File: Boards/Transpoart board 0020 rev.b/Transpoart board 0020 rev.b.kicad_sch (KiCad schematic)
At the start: 81 parts, among them J1 CEC card edge connector large, U1 6821, U1 TR1602, U10 LM311, U11 LM741, U12 LM311, U3 DM8602N, U4 7410, U4 ULN2003A, U5 74LS74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

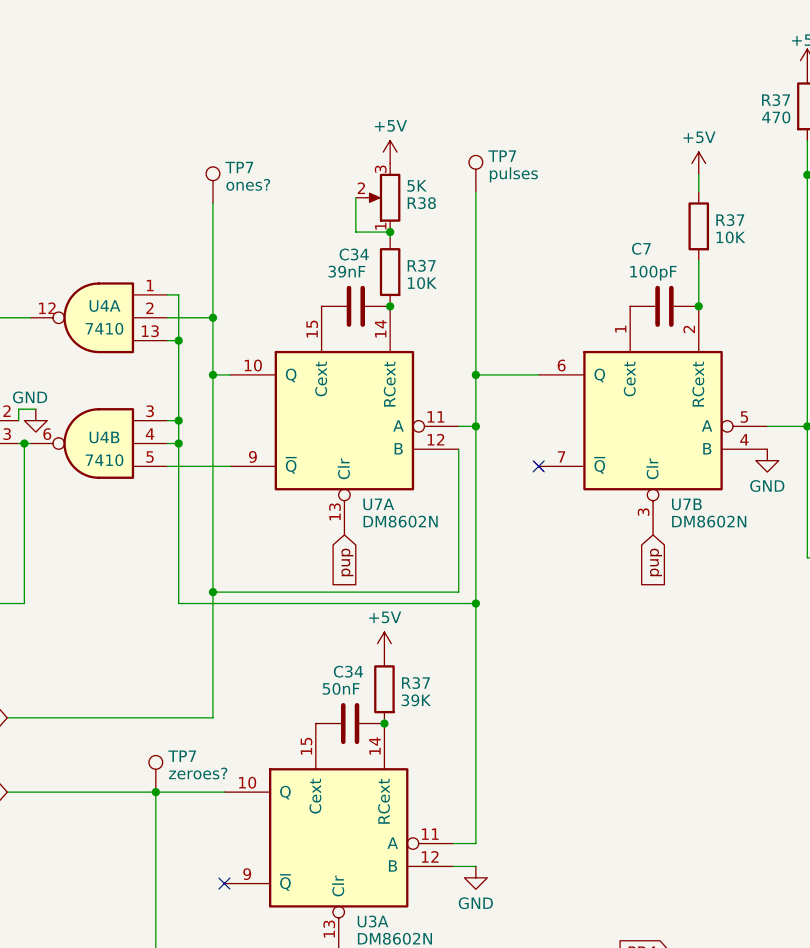
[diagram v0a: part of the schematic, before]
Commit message: revised test point names
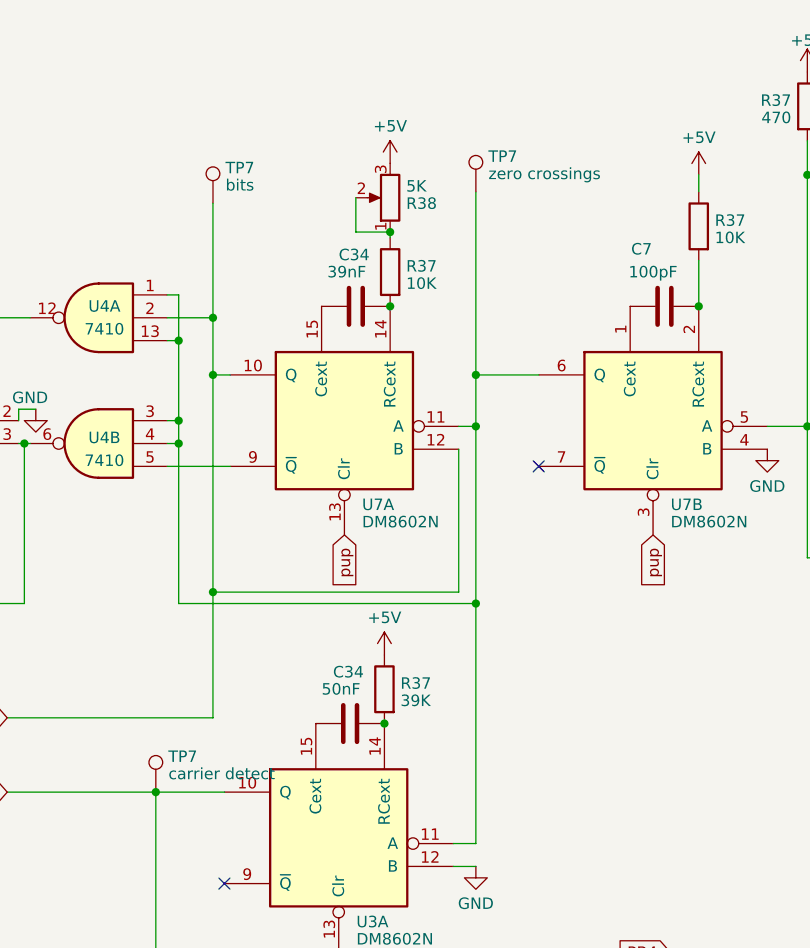
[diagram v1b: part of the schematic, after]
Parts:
- TP7: value ones? -> bits
- TP7: value pulses -> zero crossings
- TP7: value zeroes? -> carrier detect
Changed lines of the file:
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@@
       (effects (font (size 1.27 1.27)) (justify left))
     )
-    (property "Value" "ones?" (at 221.742 60.2053 0)
+    (property "Value" "bits" (at 221.742 60.2053 0)
       (effects (font (size 1.27 1.27)) (justify left))
     )
@@
       (effects (font (size 1.27 1.27)) (justify left))
     )
-    (property "Value" "pulses" (at 250.952 58.9353 0)
+    (property "Value" "zero crossings" (at 250.952 58.9353 0)
       (effects (font (size 1.27 1.27)) (justify left))
     )
@@
       (effects (font (size 1.27 1.27)) (justify left))
     )
-    (property "Value" "zeroes?" (at 215.392 125.6103 0)
-      (effects (font (size 1.27 1.27)) (justify left))
-    )
+    (property "Value" "carrier detect" (at 215.392 125.6103 0)
+      (effects (font (size 1.27 1.27)) (justify left))
+    )
